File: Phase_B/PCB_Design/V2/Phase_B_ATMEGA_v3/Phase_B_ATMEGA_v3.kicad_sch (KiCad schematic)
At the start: 49 parts, among them J1 AVR-ISP-6, J2 USB_B_Mini, J3 ESP_Conn, U1 CA56-12EWA, U2 74HC595, U3 ATmega32U4-A, U4 USBLC6-2SC6, U5 LP2985-3.3, Y1 16MHz

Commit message: Placement Update
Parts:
- added H1, H2, H3, H4: MountingHole, MountingHole:MountingHole_2.2mm_M2, symbol Mechanical:MountingHole
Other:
- note added: "Mounting Holes"
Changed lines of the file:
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@@
+    (fill (type none))
+  )
+  (rectangle (start 73.66 170.18) (end 118.745 191.135)
+    (stroke (width 0) (type dash))
     (fill (type none))
   )
@@
     (effects (font (face "KiCad Font") (size 2 2) (thickness 0.254) bold) (justify left bottom))
   )
+  (text "Mounting Holes" (at 73.66 194.31 0)
+    (effects (font (size 1.27 1.27)) (justify left bottom))
+  )
   (text "Voltage Regulator" (at 200.66 129.54 0)
     (effects (font (face "KiCad Font") (size 2 2) (thickness 0.254) bold) (justify left bottom))
@@
     )
   )
+  (symbol (lib_id "Mechanical:MountingHole") (at 76.835 173.355 0) (unit 1)
+    (in_bom yes) (on_board yes) (dnp no) (fields_autoplaced)
+    (property "Reference" "H2" (at 80.01 172.72 0)
+      (effects (font (size 1.27 1.27)) (justify left))
+    )
+    (property "Value" "MountingHole" (at 80.01 175.26 0)
+      (effects (font (size 1.27 1.27)) (justify left))
+    )
+    (property "Footprint" "MountingHole:MountingHole_2.2mm_M2" (at 76.835 173.355 0)
+      (effects (font (size 1.27 1.27)) hide)
+    )
+    (property "Datasheet" "~" (at 76.835 173.355 0)
+      (effects (font (size 1.27 1.27)) hide)
+    )
+    (instances
+      (project "Phase_B_ATMEGA_v3"
+        (path "/e63e39d7-6ac0-4ffd-8aa3-1841a4541b55"
+          (reference "H2") (unit 1)
+        )
+      )
+    )
+  )
   (symbol (lib_id "power:GND") (at 102.87 128.27 0) (unit 1)
     (in_bom yes) (on_board yes) (dnp no) (fields_autoplaced)
@@
         (path "/e63e39d7-6ac0-4ffd-8aa3-1841a4541b55"
           (reference "#PWR03") (unit 1)
+        )
+      )
+    )
+  )
+  (symbol (lib_id "Mechanical:MountingHole") (at 101.6 186.055 0) (unit 1)
+    (in_bom yes) (on_board yes) (dnp no) (fields_autoplaced)
+    (property "Reference" "H4" (at 104.775 185.42 0)
+      (effects (font (size 1.27 1.27)) (justify left))
+    )
+    (property "Value" "MountingHole" (at 104.775 187.96 0)
+      (effects (font (size 1.27 1.27)) (justify left))
+    )
+    (property "Footprint" "MountingHole:MountingHole_2.2mm_M2" (at 101.6 186.055 0)
+      (effects (font (size 1.27 1.27)) hide)
+    )
+    (property "Datasheet" "~" (at 101.6 186.055 0)
+      (effects (font (size 1.27 1.27)) hide)
+    )
+    (instances
+      (project "Phase_B_ATMEGA_v3"
+        (path "/e63e39d7-6ac0-4ffd-8aa3-1841a4541b55"
+          (reference "H4") (unit 1)
         )
       )
@@
     )
     (property "Value" "PTS125SM43SMTR21M_LFS" (at 166.37 91.44 0)
-      (effects (font (size 1.27 1.27)))
+      (effects (font (size 1.27 1.27)) hide)
     )
     (property "Footprint" "PTS125_SMD_Button:PTS125_SMD_Button" (at 177.8 92.71 0)
@@
     )
   )
+  (symbol (lib_id "Mechanical:MountingHole") (at 76.835 185.42 0) (unit 1)
+    (in_bom yes) (on_board yes) (dnp no) (fields_autoplaced)
+    (property "Reference" "H1" (at 80.01 184.785 0)
+      (effects (font (size 1.27 1.27)) (justify left))
+    )
+    (property "Value" "MountingHole" (at 80.01 187.325 0)
+      (effects (font (size 1.27 1.27)) (justify left))
+    )
+    (property "Footprint" "MountingHole:MountingHole_2.2mm_M2" (at 76.835 185.42 0)
+      (effects (font (size 1.27 1.27)) hide)
+    )
+    (property "Datasheet" "~" (at 76.835 185.42 0)
+      (effects (font (size 1.27 1.27)) hide)
+    )
+    (instances
+      (project "Phase_B_ATMEGA_v3"
+        (path "/e63e39d7-6ac0-4ffd-8aa3-1841a4541b55"
+          (reference "H1") (unit 1)
+        )
+      )
+    )
+  )
   (symbol (lib_id "Device:C_Small") (at 69.85 27.94 0) (unit 1)
     (in_bom yes) (on_board yes) (dnp no) (fields_autoplaced)
@@
         (path "/e63e39d7-6ac0-4ffd-8aa3-1841a4541b55"
           (reference "#PWR07") (unit 1)
+        )
+      )
+    )
+  )
+  (symbol (lib_id "Mechanical:MountingHole") (at 101.6 173.99 0) (unit 1)
+    (in_bom yes) (on_board yes) (dnp no) (fields_autoplaced)
+    (property "Reference" "H3" (at 104.775 173.355 0)
+      (effects (font (size 1.27 1.27)) (justify left))
+    )
+    (property "Value" "MountingHole" (at 104.775 175.895 0)
+      (effects (font (size 1.27 1.27)) (justify left))
+    )
+    (property "Footprint" "MountingHole:MountingHole_2.2mm_M2" (at 101.6 173.99 0)
+      (effects (font (size 1.27 1.27)) hide)
+    )
+    (property "Datasheet" "~" (at 101.6 173.99 0)
+      (effects (font (size 1.27 1.27)) hide)
+    )
+    (instances
+      (project "Phase_B_ATMEGA_v3"
+        (path "/e63e39d7-6ac0-4ffd-8aa3-1841a4541b55"
+          (reference "H3") (unit 1)
         )
       )
@@
     )
     (property "Value" "PTS125SM43SMTR21M_LFS" (at 166.37 68.58 0)
-      (effects (font (size 1.27 1.27)))
+      (effects (font (size 1.27 1.27)) hide)
     )
     (property "Footprint" "PTS125_SMD_Button:PTS125_SMD_Button" (at 177.8 69.85 0)

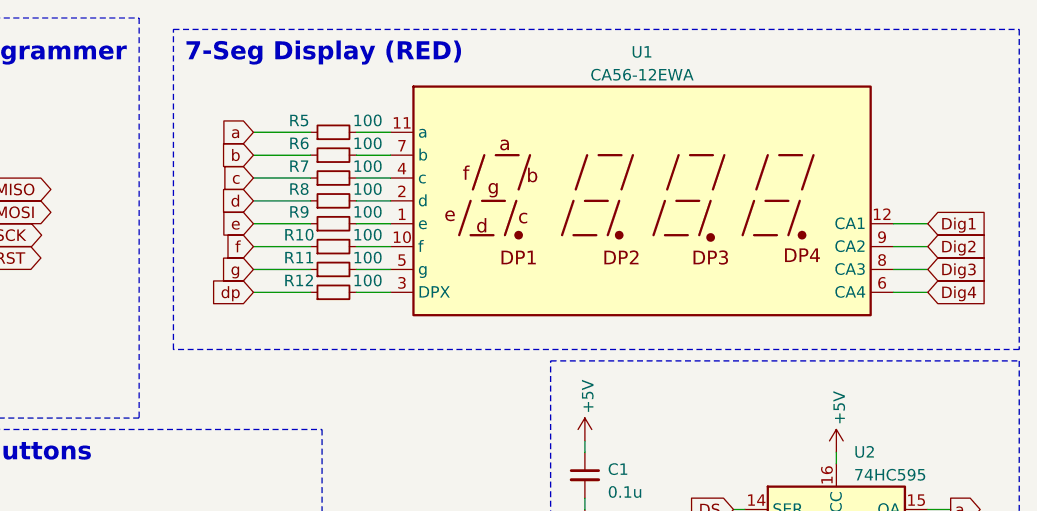
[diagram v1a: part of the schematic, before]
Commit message: Routing for V2
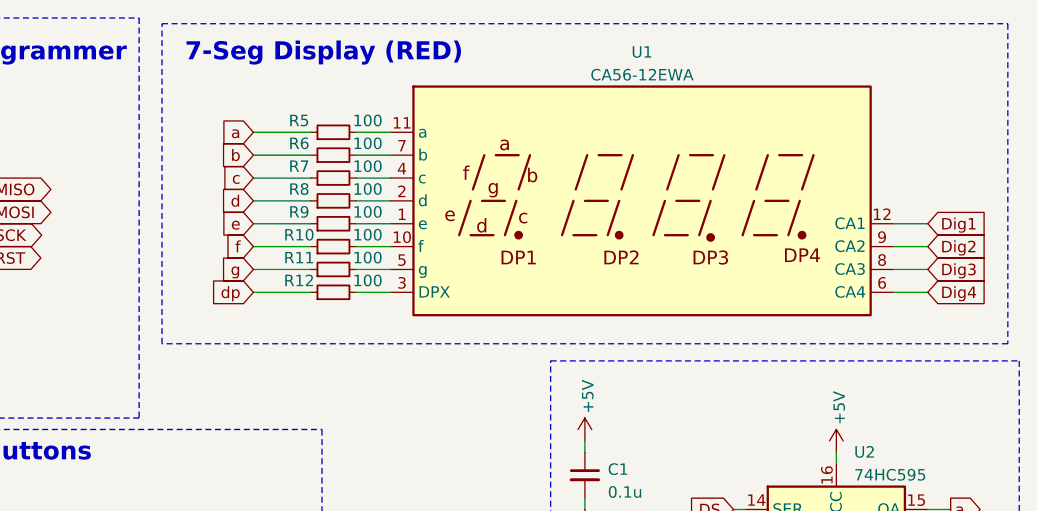
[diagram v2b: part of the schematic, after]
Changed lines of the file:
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@@
     (fill (type none))
   )
-  (rectangle (start 186.69 13.97) (end 280.67 49.53)
+  (rectangle (start 185.42 13.335) (end 279.4 48.895)
     (stroke (width 0) (type dash))
     (fill (type none))

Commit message: Phase B Update: Routing, BOM Files, Drill Files, Gerber Files, and Assembly PDF
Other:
- moved on the sheet: H3, H4
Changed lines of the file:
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@@
     )
   )
-  (symbol (lib_id "Mechanical:MountingHole") (at 101.6 186.055 0) (unit 1)
-    (in_bom yes) (on_board yes) (dnp no) (fields_autoplaced)
-    (property "Reference" "H4" (at 104.775 185.42 0)
-      (effects (font (size 1.27 1.27)) (justify left))
-    )
-    (property "Value" "MountingHole" (at 104.775 187.96 0)
-      (effects (font (size 1.27 1.27)) (justify left))
-    )
-    (property "Footprint" "MountingHole:MountingHole_2.2mm_M2" (at 101.6 186.055 0)
-      (effects (font (size 1.27 1.27)) hide)
-    )
-    (property "Datasheet" "~" (at 101.6 186.055 0)
+  (symbol (lib_id "Mechanical:MountingHole") (at 101.6 186.69 0) (unit 1)
+    (in_bom yes) (on_board yes) (dnp no) (fields_autoplaced)
+    (property "Reference" "H4" (at 104.775 186.055 0)
+      (effects (font (size 1.27 1.27)) (justify left))
+    )
+    (property "Value" "MountingHole" (at 104.775 188.595 0)
+      (effects (font (size 1.27 1.27)) (justify left))
+    )
+    (property "Footprint" "MountingHole:MountingHole_2.2mm_M2" (at 101.6 186.69 0)
+      (effects (font (size 1.27 1.27)) hide)
+    )
+    (property "Datasheet" "~" (at 101.6 186.69 0)
       (effects (font (size 1.27 1.27)) hide)
     )
@@
     )
   )
-  (symbol (lib_id "Mechanical:MountingHole") (at 101.6 173.99 0) (unit 1)
-    (in_bom yes) (on_board yes) (dnp no) (fields_autoplaced)
-    (property "Reference" "H3" (at 104.775 173.355 0)
-      (effects (font (size 1.27 1.27)) (justify left))
-    )
-    (property "Value" "MountingHole" (at 104.775 175.895 0)
-      (effects (font (size 1.27 1.27)) (justify left))
-    )
-    (property "Footprint" "MountingHole:MountingHole_2.2mm_M2" (at 101.6 173.99 0)
-      (effects (font (size 1.27 1.27)) hide)
-    )
-    (property "Datasheet" "~" (at 101.6 173.99 0)
-      (effects (font (size 1.27 1.27)) hide)
-    )
+  (symbol (lib_id "Mechanical:MountingHole") (at 100.965 174.625 0) (unit 1)
+    (in_bom yes) (on_board yes) (dnp no) (fields_autoplaced)
+    (property "Reference" "H3" (at 104.14 173.99 0)
+      (effects (font (size 1.27 1.27)) (justify left))
+    )
+    (property "Value" "MountingHole" (at 104.14 176.53 0)
+      (effects (font (size 1.27 1.27)) (justify left))
+    )
+    (property "Footprint" "MountingHole:MountingHole_2.2mm_M2" (at 100.965 174.625 0)
+      (effects (font (size 1.27 1.27)) hide)
+    )
+    (property "Datasheet" "~" (at 100.965 174.625 0)
+      (effects (font (size 1.27 1.27)) hide)
+    )

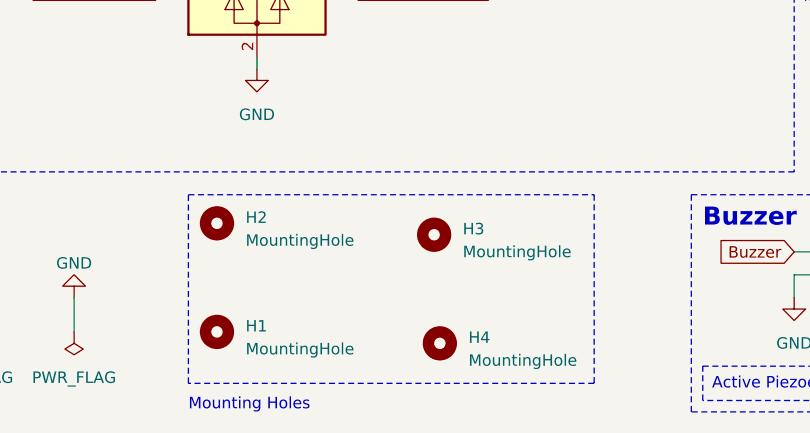
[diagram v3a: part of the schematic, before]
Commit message: Schematic Updates, 3D Model PDFs and Images added, etc.
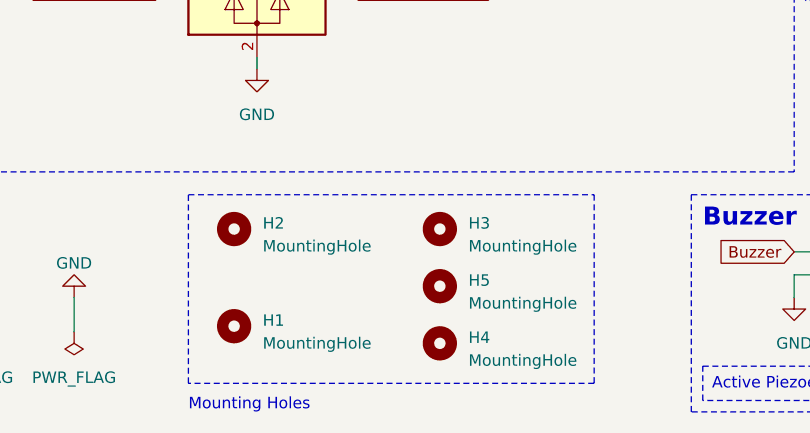
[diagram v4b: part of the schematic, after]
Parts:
- added H5: MountingHole, MountingHole:MountingHole_2.2mm_M2, symbol Mechanical:MountingHole
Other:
- moved on the sheet: H1, H2, H3
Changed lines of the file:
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@@
     )
   )
-  (symbol (lib_id "Mechanical:MountingHole") (at 76.835 173.355 0) (unit 1)
-    (in_bom yes) (on_board yes) (dnp no) (fields_autoplaced)
-    (property "Reference" "H2" (at 80.01 172.72 0)
-      (effects (font (size 1.27 1.27)) (justify left))
-    )
-    (property "Value" "MountingHole" (at 80.01 175.26 0)
-      (effects (font (size 1.27 1.27)) (justify left))
-    )
-    (property "Footprint" "MountingHole:MountingHole_2.2mm_M2" (at 76.835 173.355 0)
-      (effects (font (size 1.27 1.27)) hide)
-    )
-    (property "Datasheet" "~" (at 76.835 173.355 0)
+  (symbol (lib_id "Mechanical:MountingHole") (at 78.74 173.99 0) (unit 1)
+    (in_bom yes) (on_board yes) (dnp no) (fields_autoplaced)
+    (property "Reference" "H2" (at 81.915 173.355 0)
+      (effects (font (size 1.27 1.27)) (justify left))
+    )
+    (property "Value" "MountingHole" (at 81.915 175.895 0)
+      (effects (font (size 1.27 1.27)) (justify left))
+    )
+    (property "Footprint" "MountingHole:MountingHole_2.2mm_M2" (at 78.74 173.99 0)
+      (effects (font (size 1.27 1.27)) hide)
+    )
+    (property "Datasheet" "~" (at 78.74 173.99 0)
       (effects (font (size 1.27 1.27)) hide)
     )
@@
     )
   )
-  (symbol (lib_id "Mechanical:MountingHole") (at 76.835 185.42 0) (unit 1)
-    (in_bom yes) (on_board yes) (dnp no) (fields_autoplaced)
-    (property "Reference" "H1" (at 80.01 184.785 0)
-      (effects (font (size 1.27 1.27)) (justify left))
-    )
-    (property "Value" "MountingHole" (at 80.01 187.325 0)
-      (effects (font (size 1.27 1.27)) (justify left))
-    )
-    (property "Footprint" "MountingHole:MountingHole_2.2mm_M2" (at 76.835 185.42 0)
-      (effects (font (size 1.27 1.27)) hide)
-    )
-    (property "Datasheet" "~" (at 76.835 185.42 0)
+  (symbol (lib_id "Mechanical:MountingHole") (at 78.74 184.785 0) (unit 1)
+    (in_bom yes) (on_board yes) (dnp no) (fields_autoplaced)
+    (property "Reference" "H1" (at 81.915 184.15 0)
+      (effects (font (size 1.27 1.27)) (justify left))
+    )
+    (property "Value" "MountingHole" (at 81.915 186.69 0)
+      (effects (font (size 1.27 1.27)) (justify left))
+    )
+    (property "Footprint" "MountingHole:MountingHole_2.2mm_M2" (at 78.74 184.785 0)
+      (effects (font (size 1.27 1.27)) hide)
+    )
+    (property "Datasheet" "~" (at 78.74 184.785 0)
       (effects (font (size 1.27 1.27)) hide)
     )
@@
     )
   )
-  (symbol (lib_id "Mechanical:MountingHole") (at 100.965 174.625 0) (unit 1)
-    (in_bom yes) (on_board yes) (dnp no) (fields_autoplaced)
-    (property "Reference" "H3" (at 104.14 173.99 0)
-      (effects (font (size 1.27 1.27)) (justify left))
-    )
-    (property "Value" "MountingHole" (at 104.14 176.53 0)
-      (effects (font (size 1.27 1.27)) (justify left))
-    )
-    (property "Footprint" "MountingHole:MountingHole_2.2mm_M2" (at 100.965 174.625 0)
-      (effects (font (size 1.27 1.27)) hide)
-    )
-    (property "Datasheet" "~" (at 100.965 174.625 0)
+  (symbol (lib_id "Mechanical:MountingHole") (at 101.6 173.99 0) (unit 1)
+    (in_bom yes) (on_board yes) (dnp no) (fields_autoplaced)
+    (property "Reference" "H3" (at 104.775 173.355 0)
+      (effects (font (size 1.27 1.27)) (justify left))
+    )
+    (property "Value" "MountingHole" (at 104.775 175.895 0)
+      (effects (font (size 1.27 1.27)) (justify left))
+    )
+    (property "Footprint" "MountingHole:MountingHole_2.2mm_M2" (at 101.6 173.99 0)
+      (effects (font (size 1.27 1.27)) hide)
+    )
+    (property "Datasheet" "~" (at 101.6 173.99 0)
       (effects (font (size 1.27 1.27)) hide)
     )
@@
         )
       )
+    )
+  )
+  (symbol (lib_id "Mechanical:MountingHole") (at 101.6 180.34 0) (unit 1)
+    (in_bom yes) (on_board yes) (dnp no) (fields_autoplaced)
+    (property "Reference" "H5" (at 104.775 179.705 0)
+      (effects (font (size 1.27 1.27)) (justify left))
+    )
+    (property "Value" "MountingHole" (at 104.775 182.245 0)
+      (effects (font (size 1.27 1.27)) (justify left))
+    )
+    (property "Footprint" "MountingHole:MountingHole_2.2mm_M2" (at 101.6 180.34 0)
+      (effects (font (size 1.27 1.27)) hide)
+    )
+    (property "Datasheet" "~" (at 101.6 180.34 0)
+      (effects (font (size 1.27 1.27)) hide)
+    )
+    (instances
+      (project "Phase_B_ATMEGA_v3"
+        (path "/e63e39d7-6ac0-4ffd-8aa3-1841a4541b55"
+          (reference "H5") (unit 1)
+        )
+      )
